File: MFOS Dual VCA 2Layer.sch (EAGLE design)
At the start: 61 parts, among them IC1 TL072P, IC2 LM13700N, Q1 2N3904, Q2 2N3904, Q3 2N3906, Q4 2N3906, U1 POWER

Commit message: started the board
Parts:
- removed IN1: WQP-PJ301M-12_JACK, thonkiconn:WQP-PJ301M-12_JACK
- removed TM1, TM2: B100k, stefan-lochbrunner_EAGLE_master_custom libraries_potentiometers_Bourns PTA series_Bourns PTA series:TRIMSLIDE60
- added 1N1: AUDIO-JACKITEAD, erthenvar:AUDIO-JACKITEAD
- added LEV1, LEV2: 100k, pot:3RP/1610N
- CV1, CV2, IN2, OUT1, OUT2: value WQP-PJ301M-12_JACK -> AUDIO-JACKITEAD; device thonkiconn:WQP-PJ301M-12_JACK -> erthenvar:AUDIO-JACKITEAD
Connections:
- net +12V: now also LEV1.E, LEV2.E; no longer TM1.B, TM2.B
- net -12V: now also LEV1.A, LEV2.A; no longer TM1.A, TM2.A
- net GND: now also 1N1.RING, CV1.RING, CV2.RING, IN2.RING, OUT1.RING, OUT2.RING; no longer CV1.1, CV2.1, IN1.1, IN2.1, OUT1.1, OUT2.1
- net N$13: now also 1N1.TIP; no longer IN1.2
- net N$17: now also IN2.TIP; no longer IN2.2
- net N$19: now also OUT1.TIP; no longer OUT1.2
- net N$26: now also OUT2.TIP; no longer OUT2.2
- net N$3: now also CV1.TIP; no longer CV1.2
- net N$4: now also CV2.TIP; no longer CV2.2
- net N$5: now also LEV1.S; no longer TM1.WIPER
- net N$9: now also LEV2.S; no longer TM2.WIPER

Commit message: routed and doing labels
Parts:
- removed TRIM_A1, TRIM_A2: 2k, pot:TRIM_US-B64W
- added TRIM1, TRIM2: (no value), pot:TRIM_1234-S64YW
- BIAS1, BIAS2: value 100k -> (none); device pot:TRIM_US-B64W -> pot:TRIM_1234-S64YW
- R1, R10, R11, R12, R13, R14, R15, R16, R17, R18, R19, R2, R20, R21, R22, R23, R24, R25, R26, R27, R28, R3, R4, R5, R6, R7, R8, R9: device rcl:R-US_R1206 -> rcl:R-US_0207/7
- renumbered 1N1 to IN1
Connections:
- net +12V: now also BIAS1.E, BIAS2.E; no longer BIAS1.A, BIAS2.A
- net -12V: now also BIAS1.A, BIAS2.A; no longer BIAS1.E, BIAS2.E
- net N$22: now also TRIM1.A; no longer TRIM_A1.E
- net N$23: now also TRIM1.E, TRIM1.S; no longer TRIM_A1.A, TRIM_A1.S
- net N$29: now also TRIM2.A; no longer TRIM_A2.E
- net N$30: now also TRIM2.E, TRIM2.S; no longer TRIM_A2.A, TRIM_A2.S

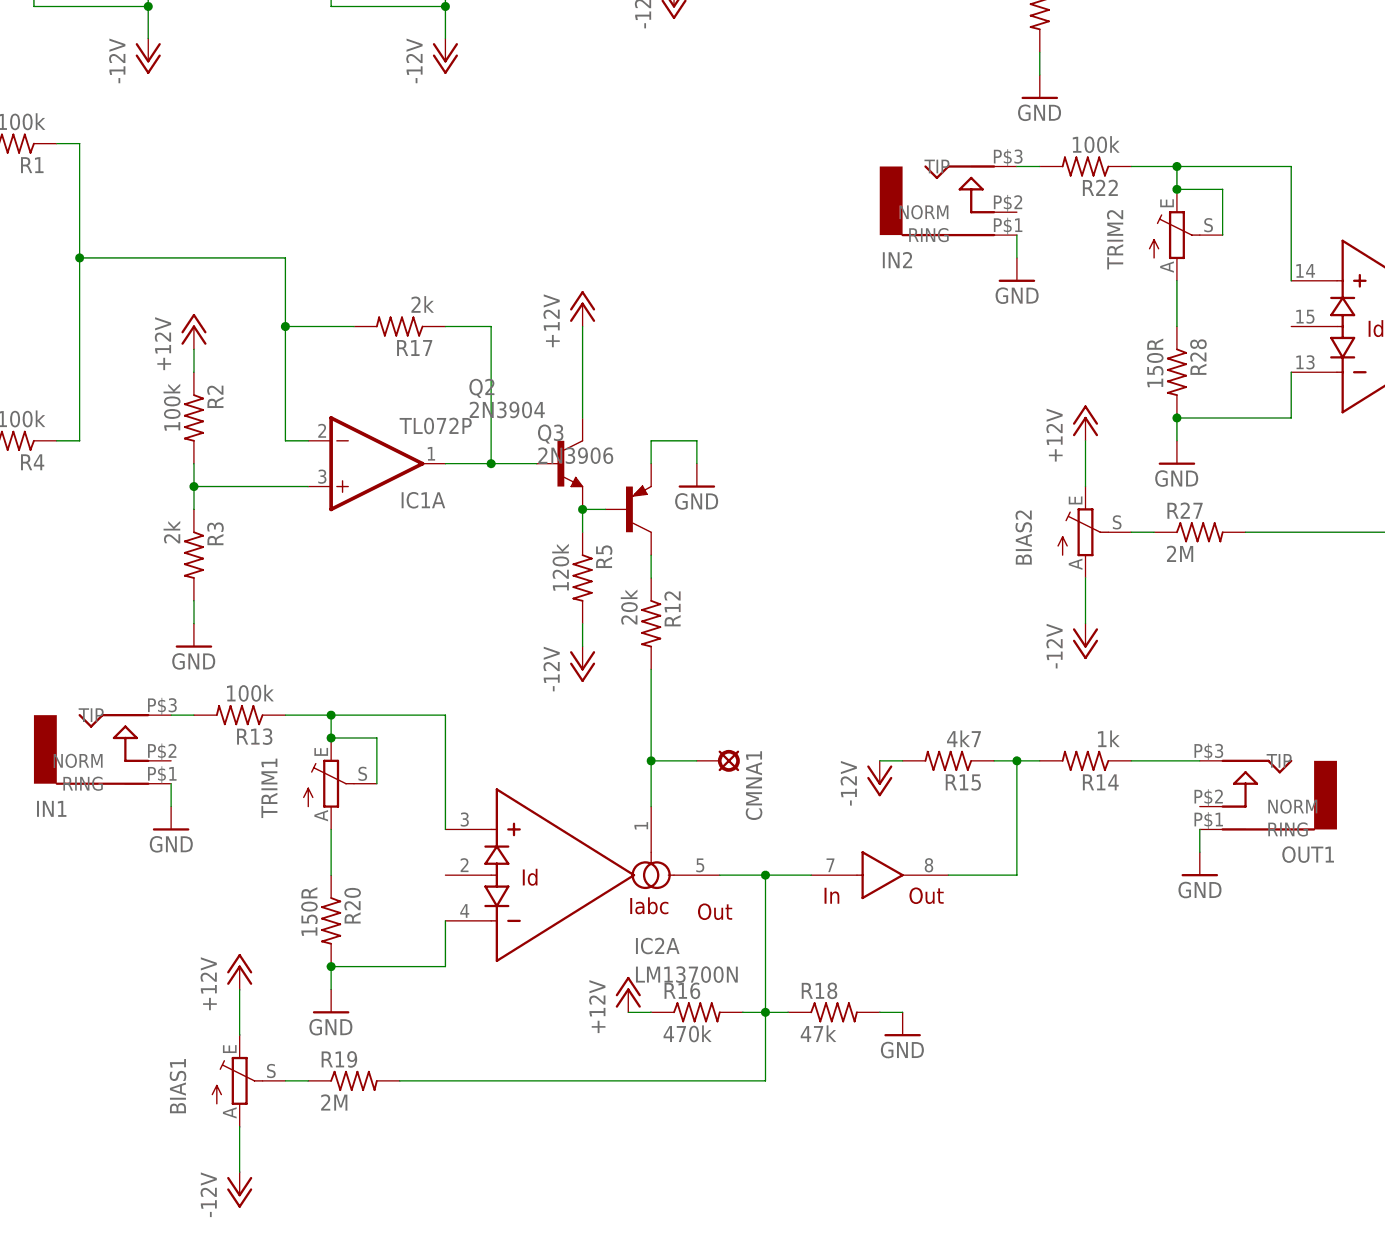
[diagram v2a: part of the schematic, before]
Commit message: switched back to custom flexitrimmers
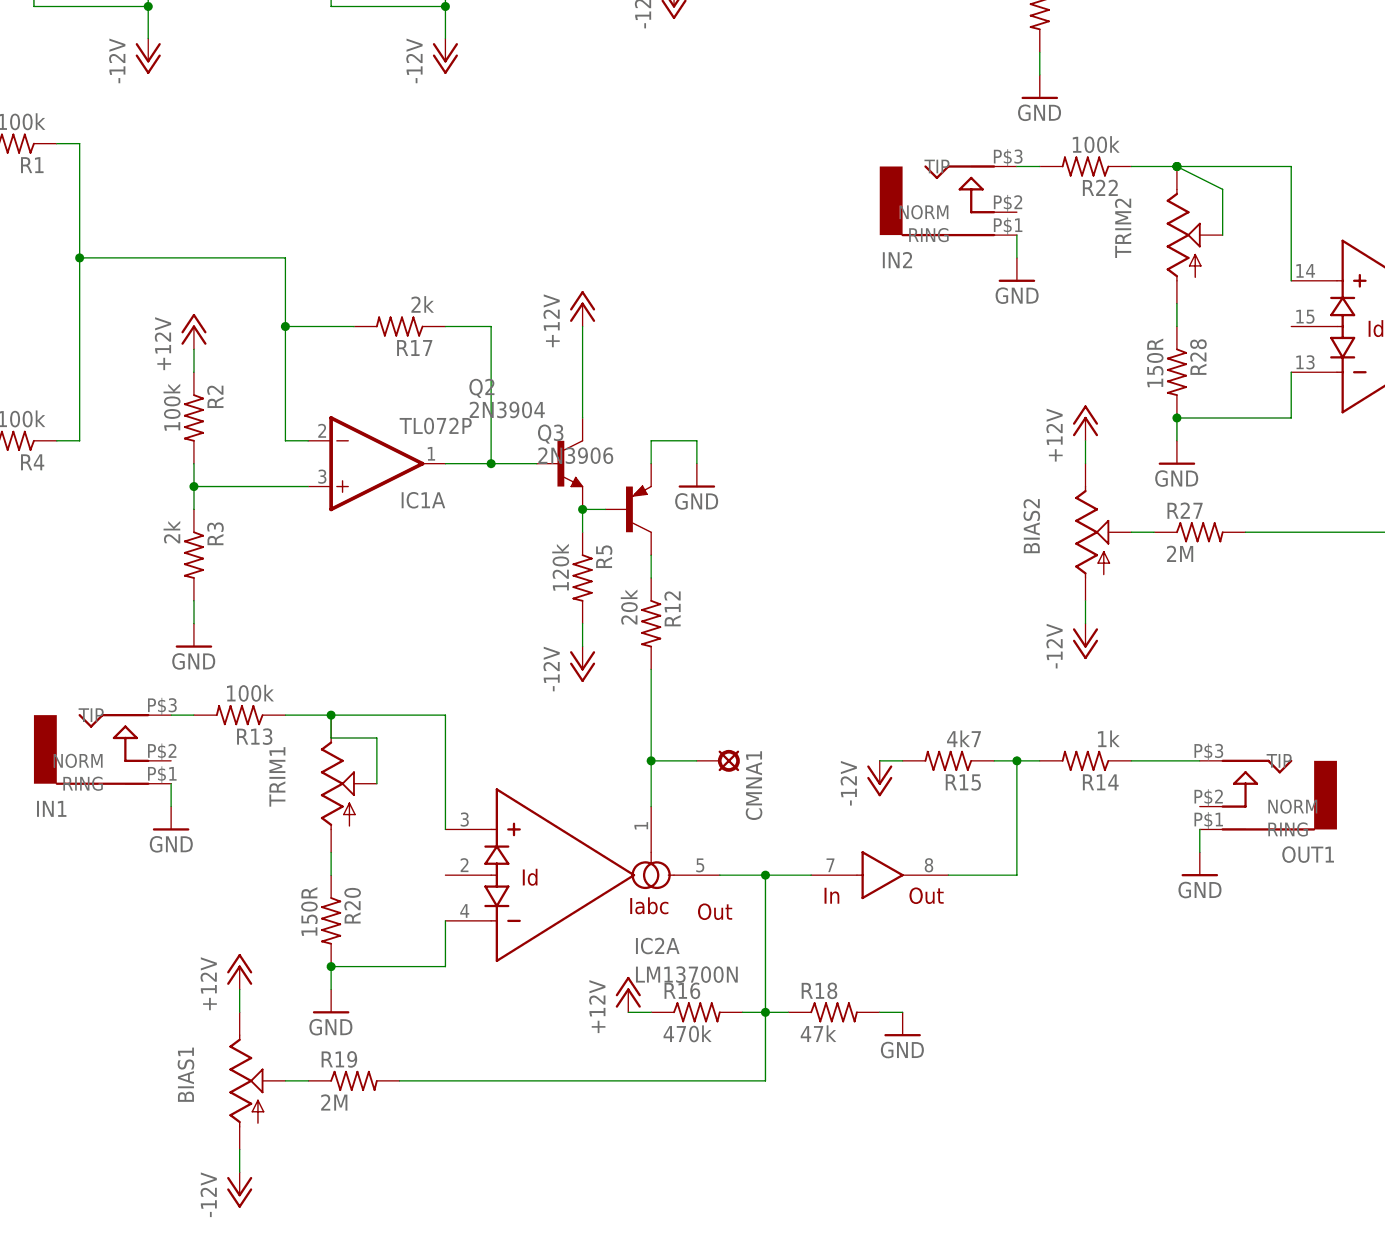
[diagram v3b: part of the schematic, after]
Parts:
- BIAS1, BIAS2, TRIM1, TRIM2: device pot:TRIM_1234-S64YW -> pot:TRIM_US-B64W

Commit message: symetric route sending to itead
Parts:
- BIAS1, BIAS2: value (none) -> 100k
- TRIM1, TRIM2: value (none) -> 2k
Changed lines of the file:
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@@
 <part name="LEV1" library="pot" deviceset="3RP/1610N" device="" value="100k"/>
 <part name="LEV2" library="pot" deviceset="3RP/1610N" device="" value="100k"/>
-<part name="BIAS1" library="pot" deviceset="TRIM_US-" device="B64W"/>
-<part name="TRIM1" library="pot" deviceset="TRIM_US-" device="B64W"/>
-<part name="TRIM2" library="pot" deviceset="TRIM_US-" device="B64W"/>
-<part name="BIAS2" library="pot" deviceset="TRIM_US-" device="B64W"/>
+<part name="BIAS1" library="pot" deviceset="TRIM_US-" device="B64W" value="100k"/>
+<part name="TRIM1" library="pot" deviceset="TRIM_US-" device="B64W" value="2k"/>
+<part name="TRIM2" library="pot" deviceset="TRIM_US-" device="B64W" value="2k"/>
+<part name="BIAS2" library="pot" deviceset="TRIM_US-" device="B64W" value="100k"/>
 </parts>
 <sheets>
